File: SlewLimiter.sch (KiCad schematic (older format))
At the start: 54 parts, among them Q101 MMBT5401, Q102 MMBT5551, Q103 MMBT5401, Q104 MMBT5551, U101 TL072, U102 TL072, U103 TL072, U104 TL072, U105 LM393

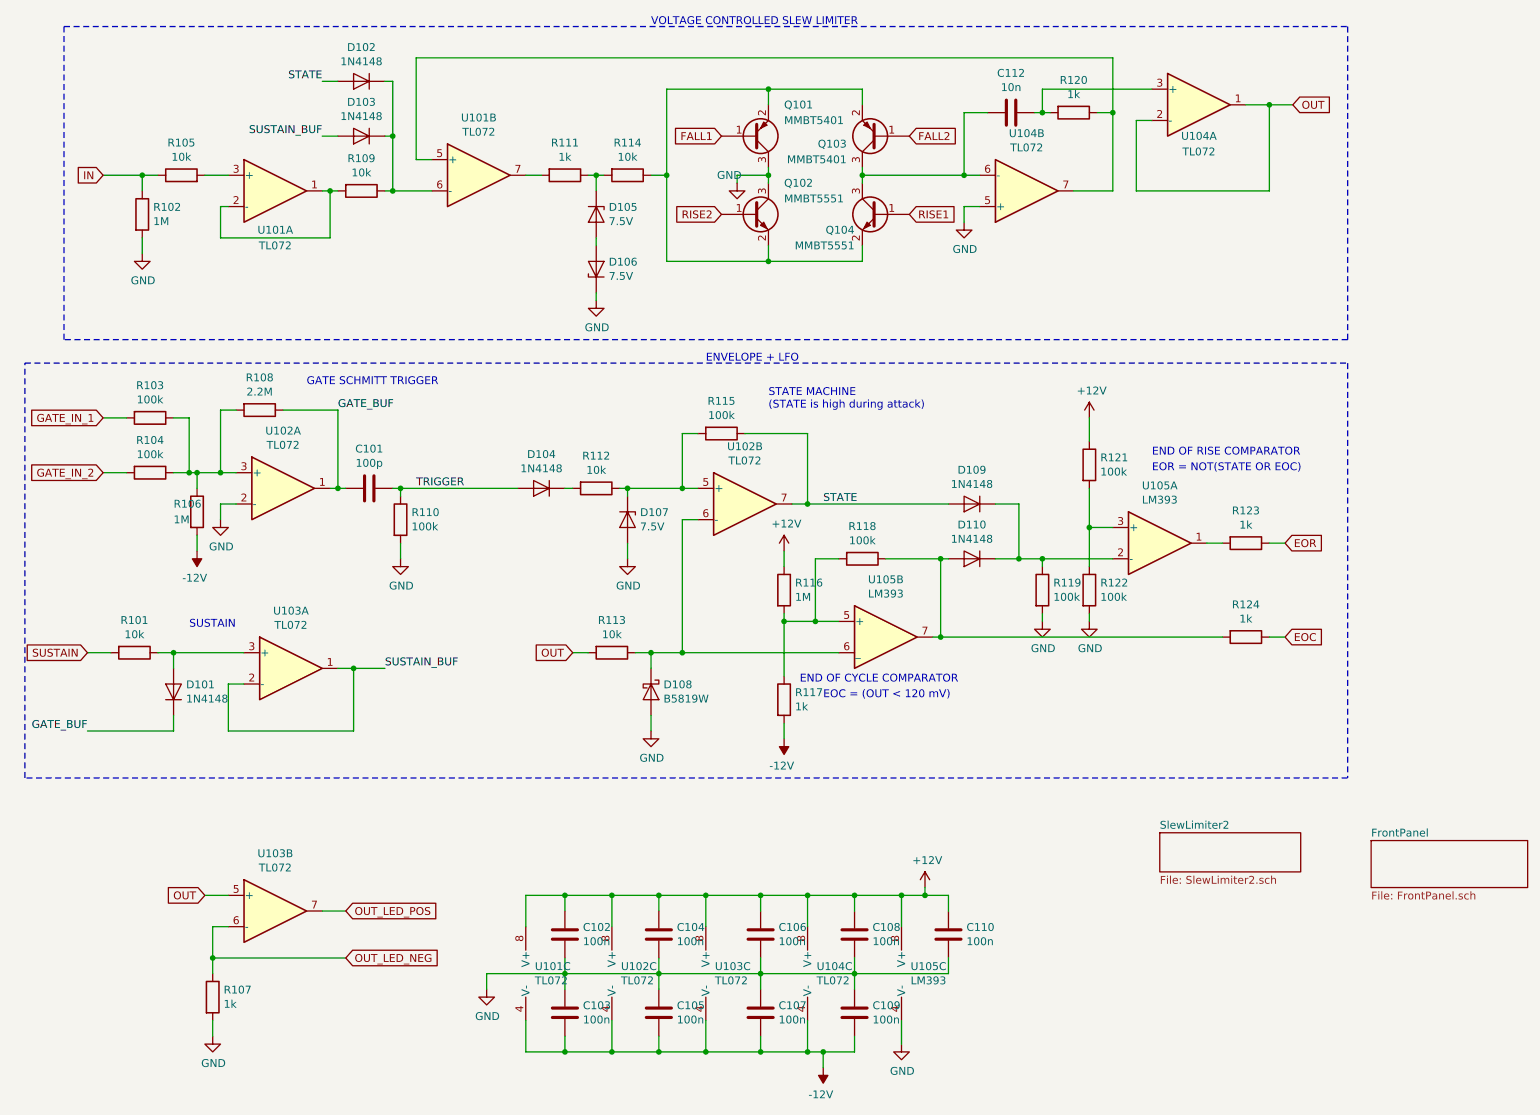
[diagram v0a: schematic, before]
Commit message: Changed EOC + terminal to go to gnd instead of -12v, added 3.3k pullup resistors to lm393 outputs
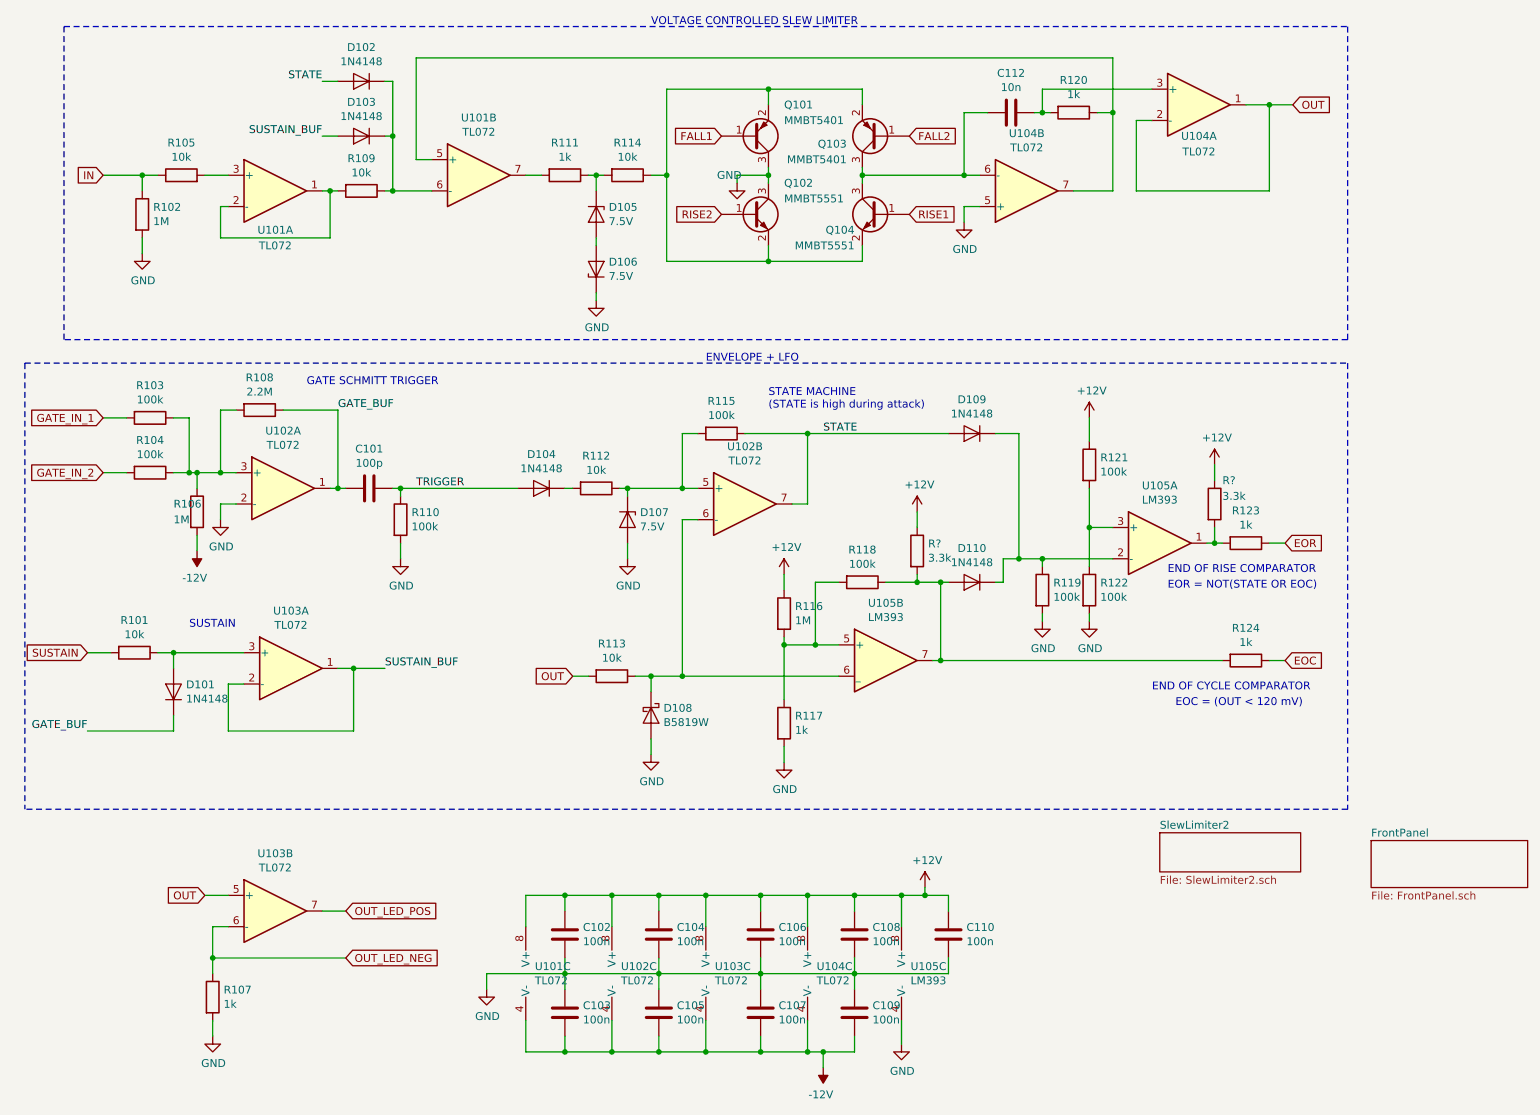
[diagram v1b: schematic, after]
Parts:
- added R? (x2): 3.3k, Resistor_SMD:R_0402_1005Metric, symbol Device:R
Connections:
- net +12V: now also R?.1, R?.1
- net -12V: no longer R117.2
- net GND: now also R117.2
- net at D110.2 (A), R118.1, R124.2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: now also R?.2
- net at R123.2, U105.1: now also R?.2
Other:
- moved on the sheet: D108, D109, D110, R113, R116, R117, R118, R124, U105B

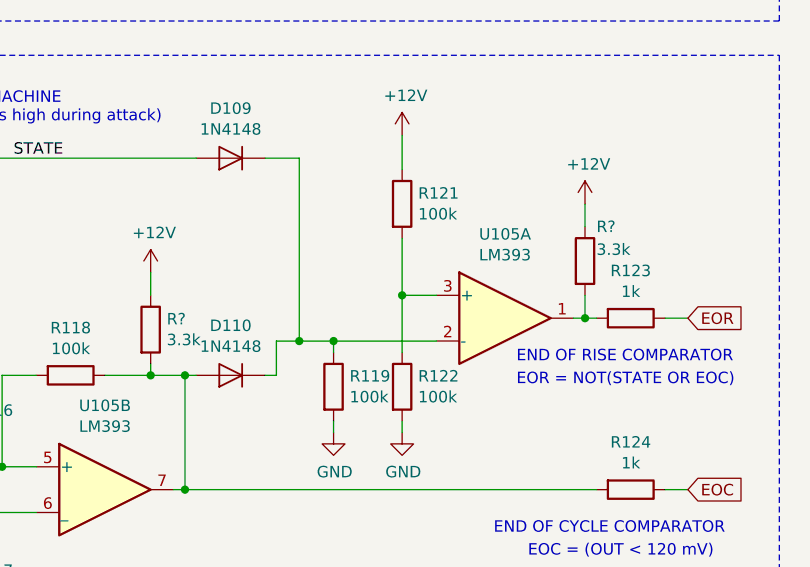
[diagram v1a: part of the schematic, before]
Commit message: Routed board with updated changes - pullup resistors on comparators, input to U105B goes to GND instead of -12V
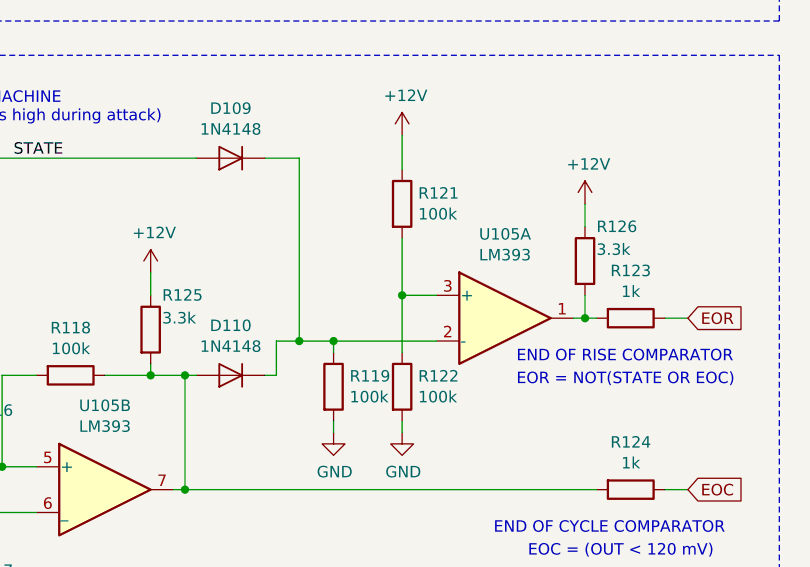
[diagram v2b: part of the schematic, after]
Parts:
- gave numbers to parts that had none: 2
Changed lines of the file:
@@
 	6300 7050 6300 7200
 $Comp
-L power:GND #PWR?
+L power:GND #PWR01
 U 1 1 61688059
 P 5550 5400
-F 0 "#PWR?" H 5550 5150 50  0001 C CNN
+F 0 "#PWR01" H 5550 5150 50  0001 C CNN
 F 1 "GND" H 5555 5227 50  0000 C CNN
 F 2 "" H 5550 5400 50  0001 C CNN
@@
 Wire Notes Line
 	700  2850 700  5700
-$Comp
-L Device:R R?
-U 1 1 617484E4
-P 6400 4050
-F 0 "R?" H 6470 4096 50  0000 L CNN
-F 1 "3.3k" H 6470 4005 50  0000 L CNN
-F 2 "Resistor_SMD:R_0402_1005Metric" V 6330 4050 50  0001 C CNN
-F 3 "~" H 6400 4050 50  0001 C CNN
-F 4 "C25890" H 6400 4050 50  0001 C CNN "LCSC"
-	1    6400 4050
-	1    0    0    -1
-$EndComp
-$Comp
-L Device:R R?
-U 1 1 61749FC9
-P 8300 3750
-F 0 "R?" H 8350 3900 50  0000 L CNN
-F 1 "3.3k" H 8350 3800 50  0000 L CNN
-F 2 "Resistor_SMD:R_0402_1005Metric" V 8230 3750 50  0001 C CNN
-F 3 "~" H 8300 3750 50  0001 C CNN
-F 4 "C25890" H 8300 3750 50  0001 C CNN "LCSC"
-	1    8300 3750
-	1    0    0    -1
-$EndComp
 Wire Wire Line
 	8300 3900 8300 4000
@@
 	8300 3500 8300 3600
 $Comp
-L power:+12V #PWR?
+L power:+12V #PWR03
 U 1 1 617B840F
 P 8300 3500
-F 0 "#PWR?" H 8300 3350 50  0001 C CNN
+F 0 "#PWR03" H 8300 3350 50  0001 C CNN
 F 1 "+12V" H 8315 3673 50  0000 C CNN
 F 2 "" H 8300 3500 50  0001 C CNN
@@
 $EndComp
 $Comp
-L power:+12V #PWR?
+L power:+12V #PWR02
 U 1 1 617B9798
 P 6400 3800
-F 0 "#PWR?" H 6400 3650 50  0001 C CNN
+F 0 "#PWR02" H 6400 3650 50  0001 C CNN
 F 1 "+12V" H 6415 3973 50  0000 C CNN
 F 2 "" H 6400 3800 50  0001 C CNN
@@
 	1    0    0    -1
 $EndComp
+$Comp
+L Device:R R126
+U 1 1 61749FC9
+P 8300 3750
+F 0 "R126" H 8350 3900 50  0000 L CNN
+F 1 "3.3k" H 8350 3800 50  0000 L CNN
+F 2 "Resistor_SMD:R_0402_1005Metric" V 8230 3750 50  0001 C CNN
+F 3 "~" H 8300 3750 50  0001 C CNN
+F 4 "C25890" H 8300 3750 50  0001 C CNN "LCSC"
+	1    8300 3750
+	1    0    0    -1
+$EndComp
+$Comp
+L Device:R R125
+U 1 1 617484E4
+P 6400 4050
+F 0 "R125" H 6450 4200 50  0000 L CNN
+F 1 "3.3k" H 6450 4100 50  0000 L CNN
+F 2 "Resistor_SMD:R_0402_1005Metric" V 6330 4050 50  0001 C CNN
+F 3 "~" H 6400 4050 50  0001 C CNN
+F 4 "C25890" H 6400 4050 50  0001 C CNN "LCSC"
+	1    6400 4050
+	1    0    0    -1
+$EndComp
